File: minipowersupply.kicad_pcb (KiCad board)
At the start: 2 copper layers, 101.4 x 60.4 mm, 90 parts, among them J1 Conn_01x01_Female, J2 Conn_01x01_Female, J3 Conn_01x01_Female, J4 Conn_01x01_Female, J5 Conn_01x01_Female, J6 Conn_01x01_Female, J7 Conn_01x01_Female, J8 Conn_01x02_Female, J9 Conn_01x02_Female, Q1 BC817, U1 ACS70331EOLCTR-2P5U3, U10 ACS70331EOLCTR-2P5U3, U11 74HC4051, U2 ACS70331EOLCTR-2P5U3, U3 ACS70331EOLCTR-2P5U3, U4 LM358, U5 74HC4051, U6 LM7805_TO220, U7 LM317L_TO92, U8 LM337L_TO92, U9 ACS70331EOLCTR-2P5U3

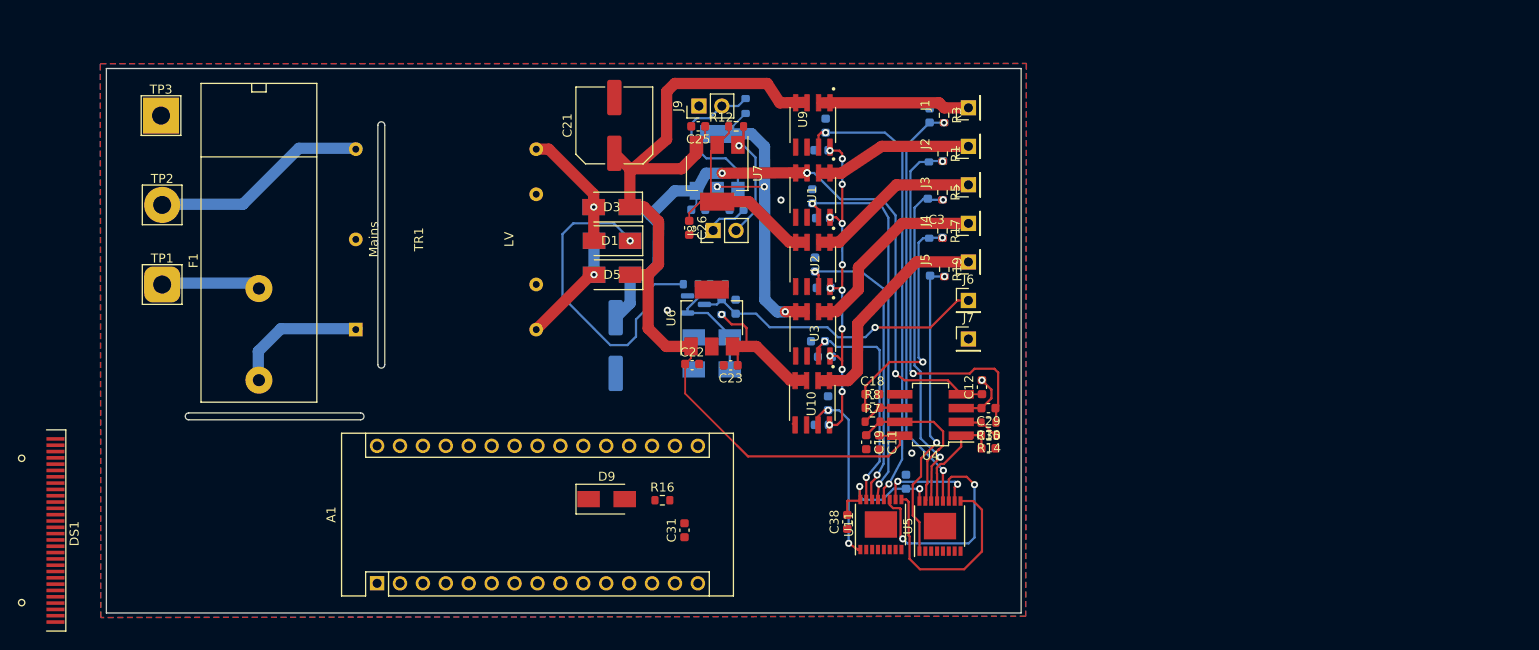
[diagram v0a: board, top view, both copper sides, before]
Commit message: Refined board and kerned size down
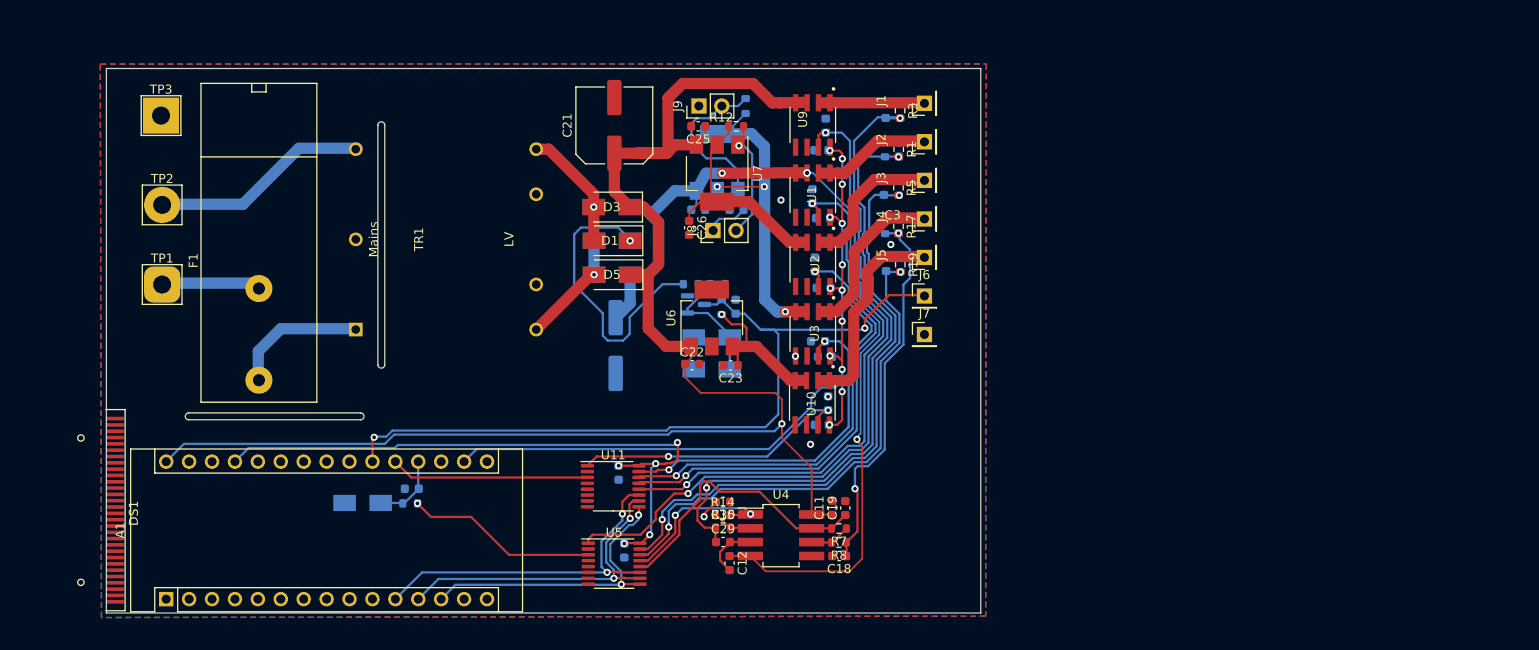
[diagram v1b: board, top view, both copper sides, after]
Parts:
- C31, C38, D9, R16: moved to B.Cu
- U11, U5: footprint Package_SO:TSSOP-16-1EP_4.4x5mm_P0.65mm -> Package_SO:TSSOP-16_4.4x5mm_P0.65mm
- moved U5 36.4 mm to (142.9, 124.8), turned to 0 degrees
- moved C12 34.1 mm to (155.7, 124.7), turned to -90 degrees
- moved C29 33.0 mm to (155.0, 122.4), turned to 0 degrees
- moved C17 31.9 mm to (143.4, 114.7), turned to 90 degrees
- moved R15 31.6 mm to (155.0, 120.8), turned to 0 degrees
- moved R14 30.8 mm to (155.0, 119.4), turned to 0 degrees
- moved C31 30.6 mm to (120.5, 116.5), turned to 0 degrees
- moved C30 30.0 mm to (155.0, 117.9), turned to 180 degrees
- moved U11 30.0 mm to (142.8, 116.2), turned to 0 degrees
- moved R16 28.0 mm to (120.3, 118.1)
- moved D9 27.1 mm to (115.0, 118.0)
- moved C38 24.9 mm to (144.1, 123.3)
- moved A1 23.4 mm to (93.3, 128.7)
- moved U4 21.3 mm to (161.4, 121.6), turned to 0 degrees
- moved C18 18.3 mm to (167.9, 123.9), turned to 180 degrees
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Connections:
- net /I V Sensor and Mux/Curent and Volt4/Isense renamed /I V Sensor and Mux/IU+
- net /I V Sensor and Mux/Curent and Volt5/Isense renamed /I V Sensor and Mux/IU-
- net /I V Sensor and Mux/Curent and Volt6/Isense renamed /I V Sensor and Mux/IA+
- net /I V Sensor and Mux/Curent and Volt7/Isense renamed /I V Sensor and Mux/IA-
- net /I V Sensor and Mux/Curent and Volt8/Isense renamed /I V Sensor and Mux/I5
- U5 pad 1: /I V Sensor and Mux/V5+i -> /I V Sensor and Mux/VU+i
- U5 pad 12: /I V Sensor and Mux/VU+i -> /I V Sensor and Mux/VA-i
- U5 pad 14: /I V Sensor and Mux/VA+i -> /I V Sensor and Mux/V5+i
- U5 pad 15: /I V Sensor and Mux/VA-i -> /I V Sensor and Mux/VA+i
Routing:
- net /Clock and TTL/VUnreg+: track 105.4 -> 170.5 mm, vias 0 -> 1
- net V5: track 14.3 -> 70.0 mm, vias 2 -> 5
- net /Clock and TTL/CK_Out: track 32.9 -> 87.9 mm, vias 1 -> 2
- net 3V3: track 37.7 -> 84.1 mm
- net /I V Sensor and Mux/VU+i: track 46.4 -> 79.8 mm
- net /I V Sensor and Mux/VA+i: track 37.7 -> 65.7 mm
- net /I V Sensor and Mux/A1: track 10.9 -> 36.5 mm
- net /I V Sensor and Mux/Unity Inverter/Ain: track 42.2 -> 67.5 mm
- net /DualAdj/VUnreg-: track 79.2 -> 103.3 mm
- net /I V Sensor and Mux/V5+i: track 33.9 -> 56.0 mm
- net /I V Sensor and Mux/Amp: track 0.00 -> 22.0 mm
- net /I V Sensor and Mux/Volt: track 0.00 -> 21.3 mm, vias 0 -> 1
- net /I V Sensor and Mux/IU+: track 51.0 -> 68.3 mm
- net /I V Sensor and Mux/IU-: track 43.1 -> 60.0 mm
- net /I V Sensor and Mux/IA+: track 34.1 -> 49.9 mm
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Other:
- board size 101.4 x 60.4 mm -> 96.9 x 60.4 mm

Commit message: further refining board size, adding rotary encoder and OLED display
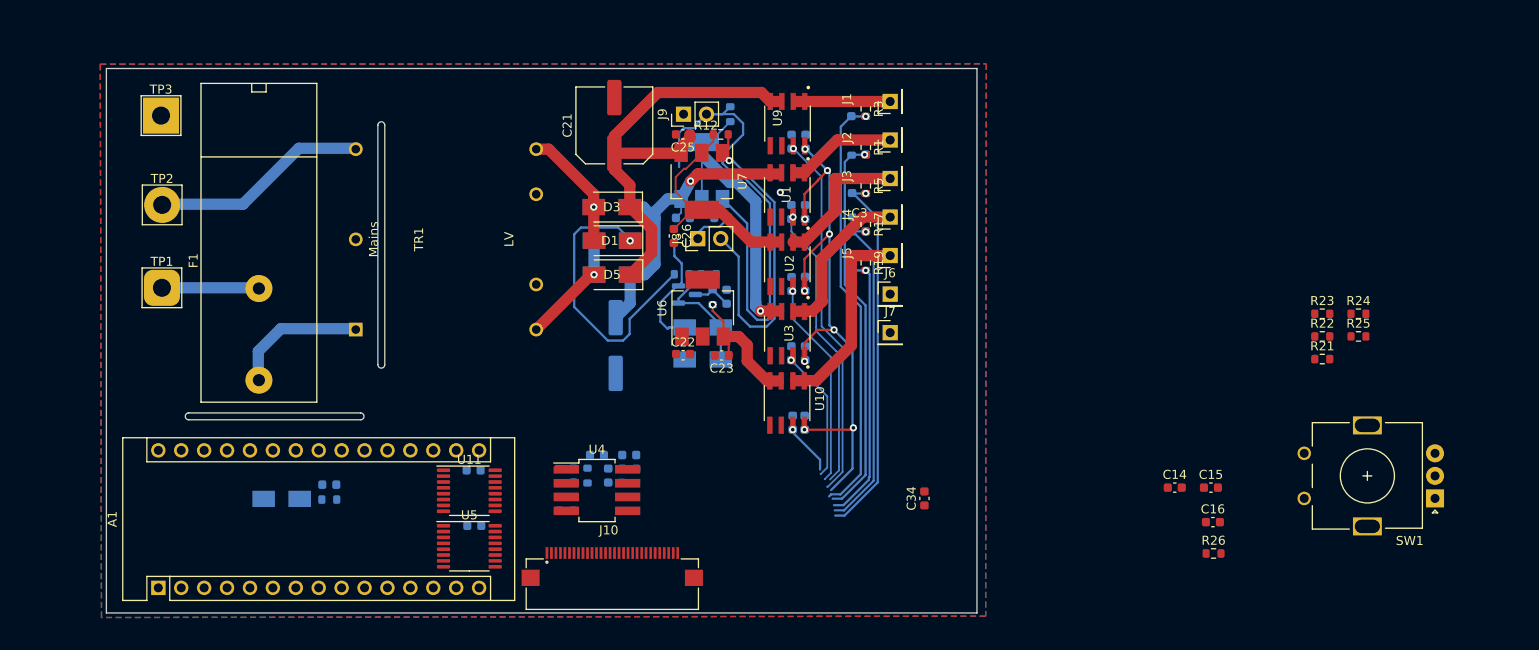
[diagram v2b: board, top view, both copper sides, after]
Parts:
- removed DS1: OLED-128O064D, Display:OLED-128O064D
- added C14: 0.1uF, Capacitor_SMD:C_0603_1608Metric, F.Cu at (205.1, 116.3)
- added C15: 0.1uF, Capacitor_SMD:C_0603_1608Metric, F.Cu at (209.1, 116.3)
- added C16: 0.1uF, Capacitor_SMD:C_0603_1608Metric, F.Cu at (209.3, 120.2)
- added C34: 0.1uF, Capacitor_SMD:C_0603_1608Metric, F.Cu at (177.3, 117.5)
- added J10: Conn_01x30_Male, WE SMD Side 30 Pin:687130149022, F.Cu at (142.7, 123.6)
- added R21: 10k, Resistor_SMD:R_0603_1608Metric, F.Cu at (221.4, 102.1)
- added R22: 10k, Resistor_SMD:R_0603_1608Metric, F.Cu at (221.4, 99.6)
- added R23: 10k, Resistor_SMD:R_0603_1608Metric, F.Cu at (221.4, 97.1)
- added R24: 10k, Resistor_SMD:R_0603_1608Metric, F.Cu at (225.4, 97.1)
- added R25: 10k, Resistor_SMD:R_0603_1608Metric, F.Cu at (225.4, 99.6)
- added R26: 10k, Resistor_SMD:R_0603_1608Metric, F.Cu at (209.4, 123.7)
- added SW1: RotaryEncoder_Switch, Rotary_Encoder:RotaryEncoder_Alps_EC11E_Vertical_H20mm, F.Cu at (233.9, 117.5)
- C11, C12, C18, C19, C29, C30, R14, R15, R7, R8: moved to B.Cu
- moved C19 26.5 mm to (142.3, 115.0)
- moved C18 25.8 mm to (144.6, 112.7)
- moved R7 24.5 mm to (143.8, 116.6), turned to 90 degrees
- moved R8 23.3 mm to (145.3, 116.6), turned to -90 degrees
- moved C11 22.9 mm to (144.6, 114.3), turned to 180 degrees
- moved U4 21.0 mm to (141.0, 116.6)
- moved C12 19.0 mm to (137.6, 118.9), turned to 0 degrees
- moved R14 18.6 mm to (136.8, 115.1), turned to 90 degrees
- moved C29 17.0 mm to (141.0, 112.7)
- moved C38 16.9 mm to (127.4, 120.6), turned to 0 degrees
- moved C30 16.8 mm to (138.4, 115.0), turned to -90 degrees
- moved U5 16.2 mm to (126.9, 122.8)
- moved R15 16.1 mm to (140.0, 115.0), turned to -90 degrees
- moved C17 16.1 mm to (127.3, 114.4), turned to 0 degrees
- moved U11 16.0 mm to (126.9, 116.7)
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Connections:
- A1 pad 1: unconnected-(A1-Pad1) -> Net-(A1-Pad1)
- A1 pad 10: unconnected-(A1-Pad10) -> /I V Sensor and Mux/A0
- A1 pad 11: /I V Sensor and Mux/A2 -> /I V Sensor and Mux/A1
- A1 pad 12: /I V Sensor and Mux/A1 -> /I V Sensor and Mux/A2
- A1 pad 13: /I V Sensor and Mux/A0 -> /I V Sensor and Mux/A3
- A1 pad 14: unconnected-(A1-Pad14) -> /I V Sensor and Mux/A4
- A1 pad 15: unconnected-(A1-Pad15) -> /I V Sensor and Mux/A5
- A1 pad 19: Net-(A1-Pad19) -> /I V Sensor and Mux/Amp
- A1 pad 2: unconnected-(A1-Pad2) -> Net-(A1-Pad2)
- A1 pad 20: /I V Sensor and Mux/Amp -> Net-(A1-Pad20)
- A1 pad 23: unconnected-(A1-Pad23) -> /Measure and Control/SDA
- A1 pad 24: unconnected-(A1-Pad24) -> /Measure and Control/SCL
- A1 pad 7: unconnected-(A1-Pad7) -> Net-(A1-Pad7)
- A1 pad 8: unconnected-(A1-Pad8) -> Net-(A1-Pad8)
- A1 pad 9: unconnected-(A1-Pad9) -> Net-(A1-Pad9)
- C31 pad 2: Net-(A1-Pad19) -> Net-(A1-Pad20)
- D9 pad 2: Net-(A1-Pad19) -> Net-(A1-Pad20)
- R16 pad 1: Net-(A1-Pad19) -> Net-(A1-Pad20)
- U11 pad 11: /I V Sensor and Mux/A2 -> /I V Sensor and Mux/A0
- U11 pad 2: unconnected-(U11-Pad2) -> GNDREF
- U11 pad 4: unconnected-(U11-Pad4) -> GNDREF
- U11 pad 5: unconnected-(U11-Pad5) -> GNDREF
- U11 pad 9: /I V Sensor and Mux/A0 -> /I V Sensor and Mux/A2
- U5 pad 10: /I V Sensor and Mux/A1 -> /I V Sensor and Mux/A4
- U5 pad 11: /I V Sensor and Mux/A2 -> /I V Sensor and Mux/A3
- U5 pad 2: unconnected-(U5-Pad2) -> GNDREF
- U5 pad 4: unconnected-(U5-Pad4) -> GNDREF
- U5 pad 5: unconnected-(U5-Pad5) -> GNDREF
- U5 pad 9: /I V Sensor and Mux/A0 -> /I V Sensor and Mux/A5
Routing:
- net /Clock and TTL/VUnreg+: track 170.5 -> 48.8 mm, vias 1 -> 0
- net /Clock and TTL/CK_Out: track 87.9 -> 4.32 mm, vias 2 -> 0
- net V5: track 70.0 -> 0.00 mm, vias 5 -> 0
- net /DualAdj/VUnreg-: track 103.3 -> 36.0 mm, vias 4 -> 1
- net /I V Sensor and Mux/A2: track 39.6 -> 0.00 mm, vias 2 -> 0
- net Net-(J9-Pad2): track 18.0 -> 57.0 mm
- net /I V Sensor and Mux/A1: track 36.5 -> 0.00 mm, vias 2 -> 0
- net /I V Sensor and Mux/A0: track 33.4 -> 0.00 mm, vias 2 -> 0
- net /I V Sensor and Mux/VU+i: track 79.8 -> 47.3 mm, vias 2 -> 1
- net /I V Sensor and Mux/VA-i: track 31.3 -> 0.89 mm
- net /I V Sensor and Mux/IU+: track 68.3 -> 40.5 mm, vias 2 -> 1
- net /I V Sensor and Mux/IA+: track 49.9 -> 23.0 mm, vias 2 -> 1
- net /I V Sensor and Mux/IU-: track 60.0 -> 33.2 mm, vias 2 -> 1
- net /I V Sensor and Mux/I5: track 32.0 -> 5.65 mm, vias 2 -> 1
- net /I V Sensor and Mux/V5+i: track 56.0 -> 30.1 mm, vias 2 -> 1
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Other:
- board size 96.9 x 60.4 mm -> 96.5 x 60.4 mm

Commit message: repositioned signal wires and started mapping OLED and rotary encoder
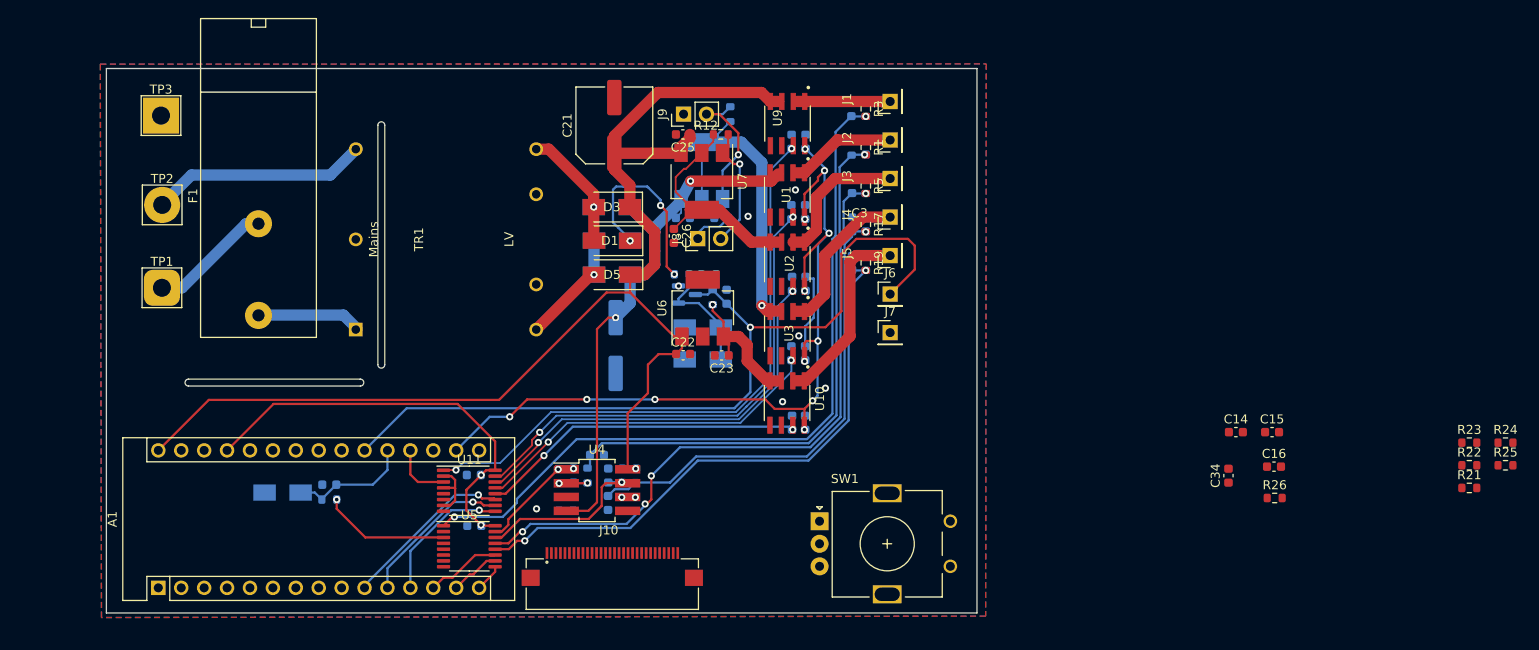
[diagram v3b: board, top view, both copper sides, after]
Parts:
- moved SW1 68.3 mm to (165.7, 120.1), turned to 0 degrees
- moved C34 33.8 mm to (211.0, 115.0)
- moved R24 21.7 mm to (241.7, 111.4)
- moved R25 21.7 mm to (241.7, 113.9)
- moved R21 21.7 mm to (237.7, 116.4)
- moved R22 21.7 mm to (237.7, 113.9)
- moved R23 21.7 mm to (237.7, 111.4)
- moved R26 9.15 mm to (216.2, 117.5)
- moved C14 9.15 mm to (211.8, 110.2)
- moved C15 9.15 mm to (215.9, 110.2)
- moved C16 9.15 mm to (216.1, 114.0)
- moved F1 7.18 mm to (103.5, 97.3)
- moved C18 5.81 mm to (142.2, 118.0), turned to -90 degrees
- moved D9 0.71 mm to (106.2, 116.9)
- moved C17 0.53 mm to (127.4, 115.0)
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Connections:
- A1 pad 1: Net-(A1-Pad1) -> unconnected-(A1-Pad1)
- A1 pad 2: Net-(A1-Pad2) -> unconnected-(A1-Pad2)
- A1 pad 23: /Measure and Control/SDA -> /Measure and Display/SDA
- A1 pad 24: /Measure and Control/SCL -> /Measure and Display/SCL
- J10 pad 10: Net-(A1-Pad2) -> /Measure and Display/SCL
- J10 pad 11: Net-(A1-Pad1) -> /Measure and Display/SDA
- U11 pad 1: /I V Sensor and Mux/I5 -> /I V Sensor and Mux/IU+
- U11 pad 12: /I V Sensor and Mux/IU+ -> /I V Sensor and Mux/I5
- U11 pad 13: /I V Sensor and Mux/IU- -> /I V Sensor and Mux/IA-
- U11 pad 15: /I V Sensor and Mux/IA- -> /I V Sensor and Mux/IU-
- U5 pad 12: /I V Sensor and Mux/VA-i -> /I V Sensor and Mux/V5+i
- U5 pad 13: /I V Sensor and Mux/VU-i -> /I V Sensor and Mux/VA+i
- U5 pad 14: /I V Sensor and Mux/V5+i -> /I V Sensor and Mux/VA-i
- U5 pad 15: /I V Sensor and Mux/VA+i -> /I V Sensor and Mux/VU-i
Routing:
- net /Clock and TTL/CK_Out: track 4.32 -> 93.5 mm, vias 0 -> 1
- net /Clock and TTL/VUnreg+: track 48.8 -> 137.7 mm, vias 0 -> 1
- net V5: track 0.00 -> 47.0 mm, vias 0 -> 2
- net Net-(J9-Pad2): track 57.0 -> 15.4 mm, vias 0 -> 1
- net /I V Sensor and Mux/VU+i: track 47.3 -> 84.0 mm, vias 1 -> 2
- net /I V Sensor and Mux/V5+i: track 30.1 -> 64.2 mm, vias 1 -> 2
- net /I V Sensor and Mux/VA+i: track 41.3 -> 72.8 mm, vias 1 -> 4
- net /I V Sensor and Mux/I5: track 5.65 -> 36.2 mm, vias 1 -> 2
- net /I V Sensor and Mux/IU+: track 40.5 -> 66.8 mm, vias 1 -> 2
- net 3V3: track 65.0 -> 90.9 mm, vias 9 -> 12
- net /DualAdj/VUnreg-: track 36.0 -> 61.2 mm, vias 1 -> 2
- net /I V Sensor and Mux/IA-: track 14.6 -> 39.5 mm, vias 1 -> 2
- net /I V Sensor and Mux/IA+: track 23.0 -> 46.8 mm, vias 1 -> 2
- net /I V Sensor and Mux/IU-: track 33.2 -> 56.0 mm, vias 1 -> 2
- net Net-(J8-Pad2): track 37.5 -> 15.0 mm
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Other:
- outline, holes or cut-outs redrawn
